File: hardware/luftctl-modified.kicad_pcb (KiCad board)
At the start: 2 copper layers, 56.6 x 32 mm, 43 parts, among them J1 USB_C_Receptacle_USB2.0, J4 PWM Fan, J5 PWM Fan, J6 Conn_01x10, SW1 Reset, U3 USBLC6-4SC6, U4 ESP32-C3-WROOM-02, U5 CH224K, U6 LMR51420YFDDCR

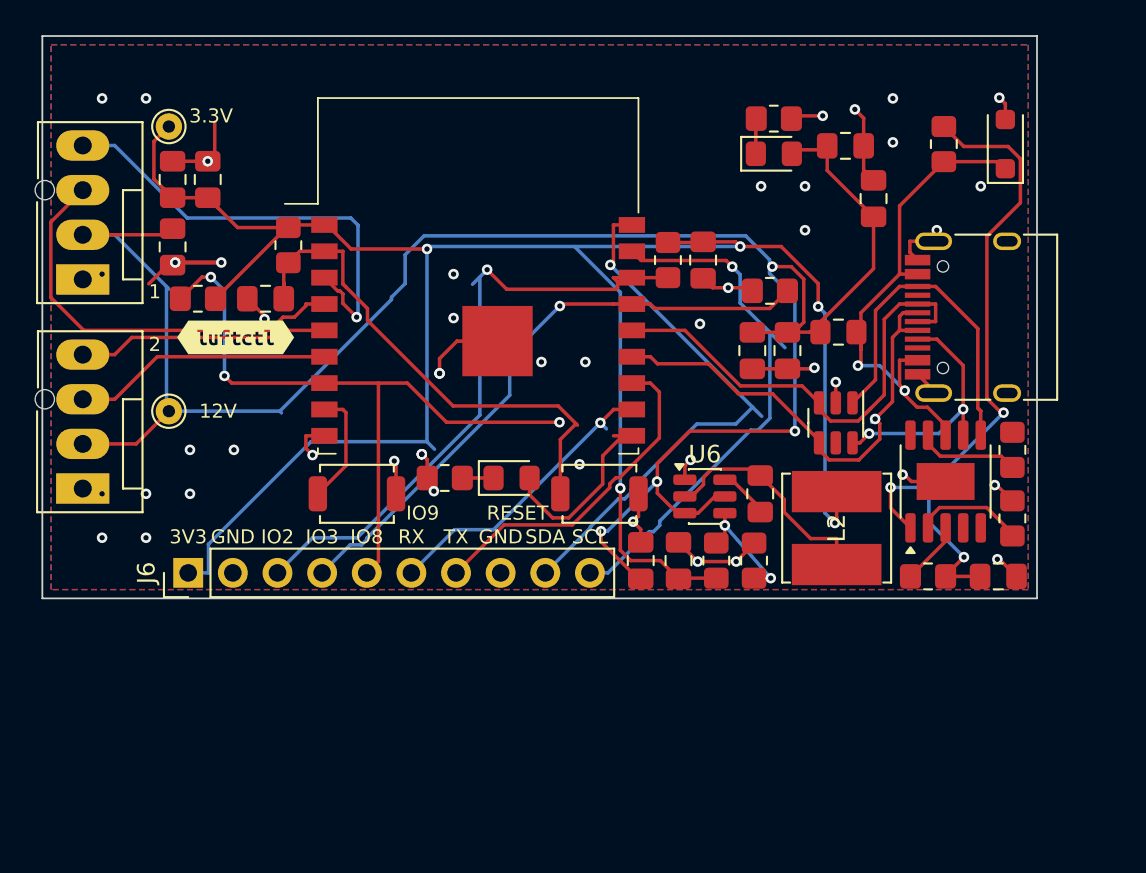
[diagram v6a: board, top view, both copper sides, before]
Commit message: Add J7/J8 switch headers (GPIO3, GPIO8) beside USB-C
- J7 (GPIO3+GND) above and J8 (GPIO8+GND) below the USB-C port on the
  right edge; ESPHome Switch 1/Switch 2 binary sensors with pull-ups.
- Remove R3 (old GPIO3 pull-down) so the switch input can idle high.
- J6 back to 8 pins (3V3, GND, IO2, RX, TX, GND, SDA, SCL).
- Tie CH224K CFG1/CFG2 directly to GND; drop R13/R14 0R straps.
- Edge no-track strips; FAN1_Tacho re-routed off the board edge.
- DRC 0 unconnected, no new errors; board matches schematic.

Co-Authored-By: Claude Opus 5.5 (1M context) <noreply@anthropic.com>
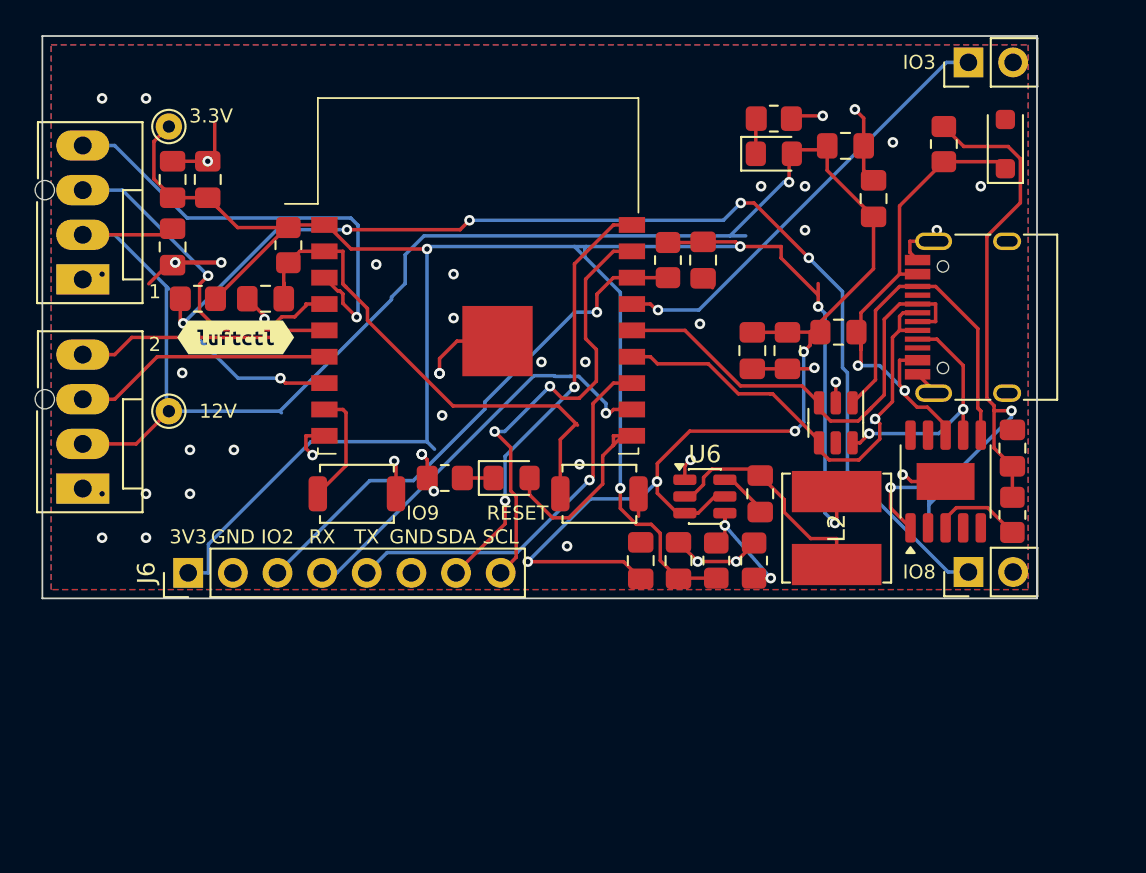
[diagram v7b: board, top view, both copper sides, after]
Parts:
- removed R13, R14: 0Ω, R_0805_2012Metric_Pad1.20x1.40mm_HandSolder
- removed R3: 10kΩ, Resistor_SMD:R_0805_2012Metric_Pad1.20x1.40mm_HandSolder
- added J7: SW_IO3, PinHeader_1x02_P2.54mm_Vertical, F.Cu at (178.3, 48.0)
- added J8: SW_IO8, PinHeader_1x02_P2.54mm_Vertical, F.Cu at (178.3, 77.0)
- J6: value Conn_01x10 -> Conn_01x08; footprint PinHeader_1x10_P2.54mm_Vertical -> PinHeader_1x08_P2.54mm_Vertical
- moved C15 7.34 mm to (180.8, 69.9), turned to 90 degrees
- moved R15 5.94 mm to (180.8, 73.7), turned to 90 degrees
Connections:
- J6 pad 4: GPIO3 -> RXD
- J6 pad 5: GPIO8 -> TXD
- J6 pad 6: RXD -> GND
- J6 pad 7: TXD -> SDA
- J6 pad 8: GND -> SCL
- U5 pad 2: CFG2 -> GND
- U5 pad 9: CFG1 -> GND
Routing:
- net GPIO8: track 39.4 -> 73.0 mm, vias 3 -> 6
- net GPIO3: track 35.8 -> 25.1 mm
- net GND: track 56.6 -> 48.2 mm, vias 47 -> 45
- net SDA: track 31.4 -> 24.6 mm, vias 1 -> 2
- net RXD: track 16.9 -> 23.6 mm
- net CFG2: track 6.33 -> 0.00 mm
- net GPIO2: track 36.0 -> 30.0 mm
- net CFG1: track 5.85 -> 0.00 mm
- net SCL: track 31.3 -> 25.8 mm, vias 1 -> 2
- net FAN1_Tacho: track 23.9 -> 19.6 mm, vias 0 -> 1
- net VDD_CH: track 40.1 -> 43.5 mm, vias 3 -> 2
- net TXD: track 19.3 -> 22.0 mm, vias 0 -> 1
- net +12V: track 123.1 -> 125.6 mm, vias 4 -> 5
- net CFG3: track 3.59 -> 5.17 mm
- net +3V3: track 124.3 -> 125.1 mm
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
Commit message: J7/J8 vertical along the USB-C edge; board 3 mm wider (59.75 x 32.1)
Both switch headers now stand vertically on the right edge above and below
USB-C (GND pins nearest the port). Right edge moved out 3 mm; J1 moved with
it. Re-routed; DRC 0 unconnected, no new violations; CPL/gerbers updated.

Co-Authored-By: Claude Opus 5.5 (1M context) <noreply@anthropic.com>
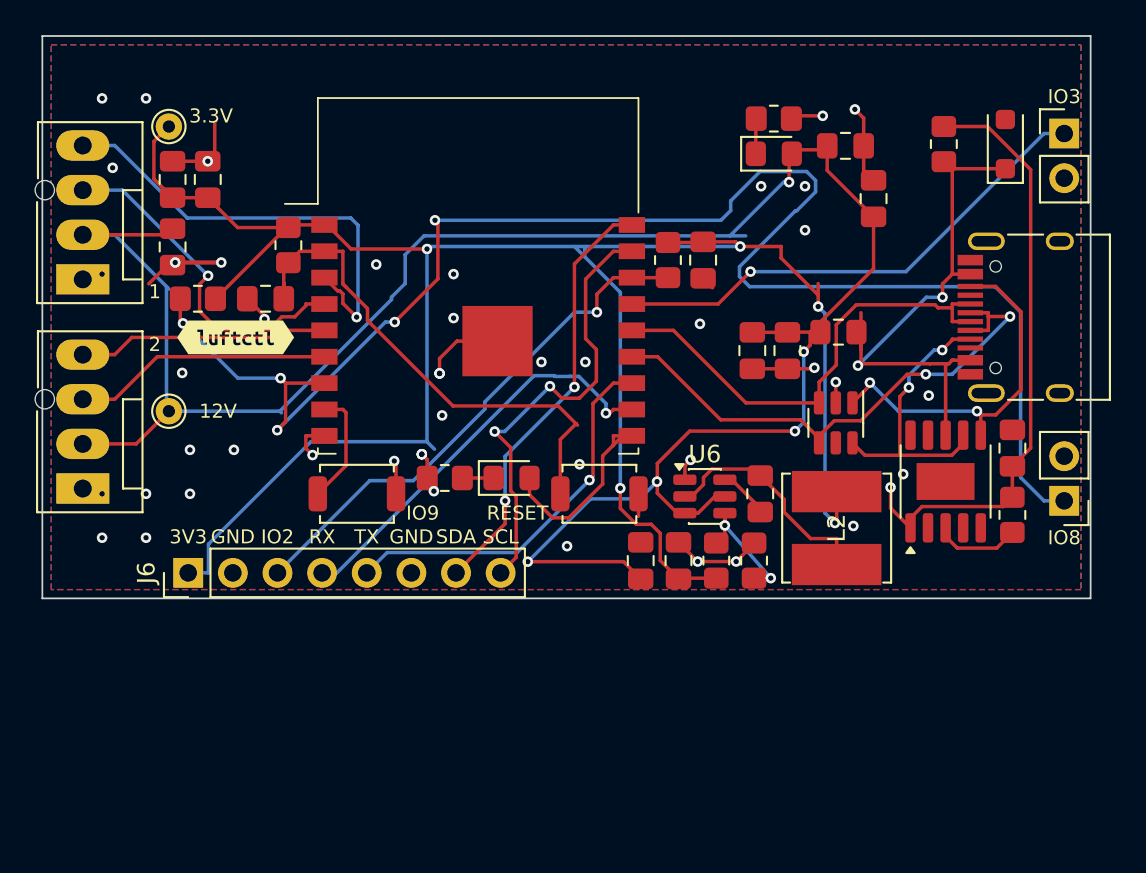
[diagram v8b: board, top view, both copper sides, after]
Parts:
- moved J7 6.79 mm to (183.8, 52.0), turned to 0 degrees
- moved J8 6.79 mm to (183.8, 72.9), turned to 180 degrees
- moved J1 3.00 mm to (182.4, 62.5)
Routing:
- net GPIO8: track 73.0 -> 89.8 mm, vias 6 -> 5
- net VDD_CH: track 43.5 -> 34.6 mm, vias 2 -> 1
- net GND: track 48.2 -> 41.5 mm
- net VBUS: track 29.5 -> 33.4 mm
- net GPIO3: track 25.1 -> 28.6 mm
- net USB-: track 27.7 -> 30.9 mm, vias 1 -> 2
- net CC1: track 14.3 -> 16.5 mm
- net CC2: track 19.5 -> 20.6 mm, vias 0 -> 2
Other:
- board size 56.6 x 32 mm -> 59.7 x 32 mm
